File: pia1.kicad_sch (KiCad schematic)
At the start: 33 parts, among them IC20 MC14529B, IC24 74LS244N, IC25 LM393P, IC26 MC6821

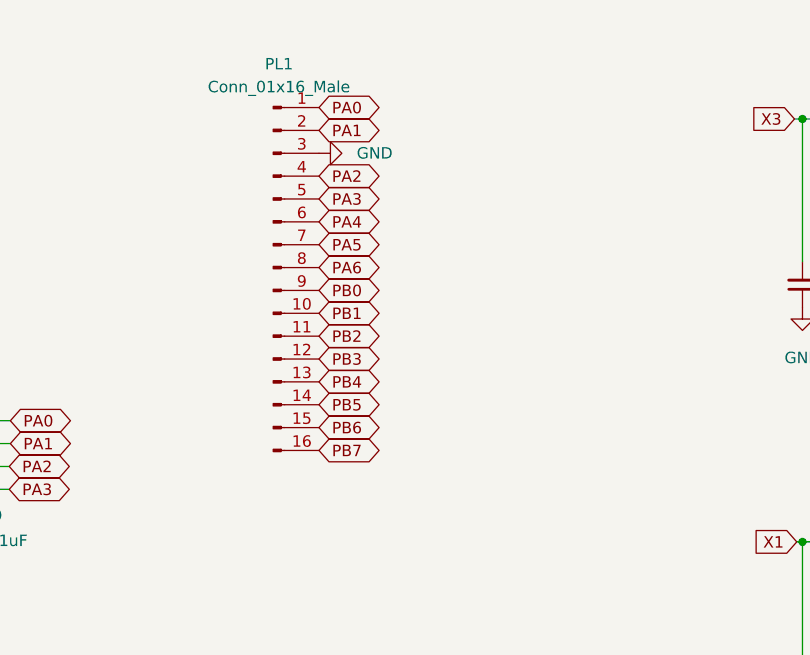
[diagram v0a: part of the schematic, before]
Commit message: add power pin to keyboard connection
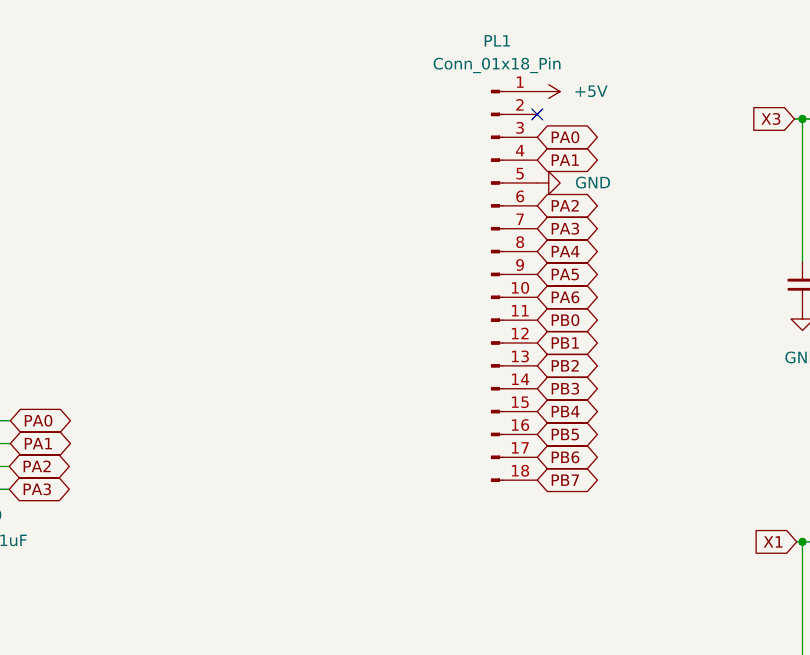
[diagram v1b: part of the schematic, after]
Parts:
- removed PL1: Conn_01x16_Male, Connector_PinHeader_2.54mm:PinHeader_1x16_P2.54mm_Vertical, symbol Connector:Conn_01x16_Male
- added PL1: Conn_01x18_Pin, Connector_PinHeader_2.54mm:PinHeader_1x18_P2.54mm_Vertical, symbol Connector:Conn_01x18_Pin
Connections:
- net +5V: now also PL1.1 (Pin_1)
- net GND: now also PL1.5 (Pin_5)
- net PA0: now also PL1.3 (Pin_3)
- net PA1: now also PL1.4 (Pin_4)
- net PA2: now also PL1.6 (Pin_6)
- net PA3: now also PL1.7 (Pin_7)
- net PA4: now also PL1.8 (Pin_8)
- net PA5: now also PL1.9 (Pin_9)
- net PA6: now also PL1.10 (Pin_10)
- net PB0: now also PL1.11 (Pin_11)
- net PB1: now also PL1.12 (Pin_12)
- net PB2: now also PL1.13 (Pin_13)
- net PB3: now also PL1.14 (Pin_14)
- net PB4: now also PL1.15 (Pin_15)
- net PB5: now also PL1.16 (Pin_16)
- net PB6: now also PL1.17 (Pin_17)
- net PB7: now also PL1.18 (Pin_18)
- no-connect marks 0 -> 1

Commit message: reinforce audio traces
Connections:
- net P0 renamed ~{P0}
